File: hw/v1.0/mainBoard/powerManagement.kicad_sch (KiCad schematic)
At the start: 23 parts, among them J10 Conn_01x01, J16 Battery_voltage, J9 Conn_01x01, Q10 AO3401A, Q11 2N7002, Q12 AO3401A, Q13 2N7002, Q9 AO3401A, U3 AMS1117-3.3

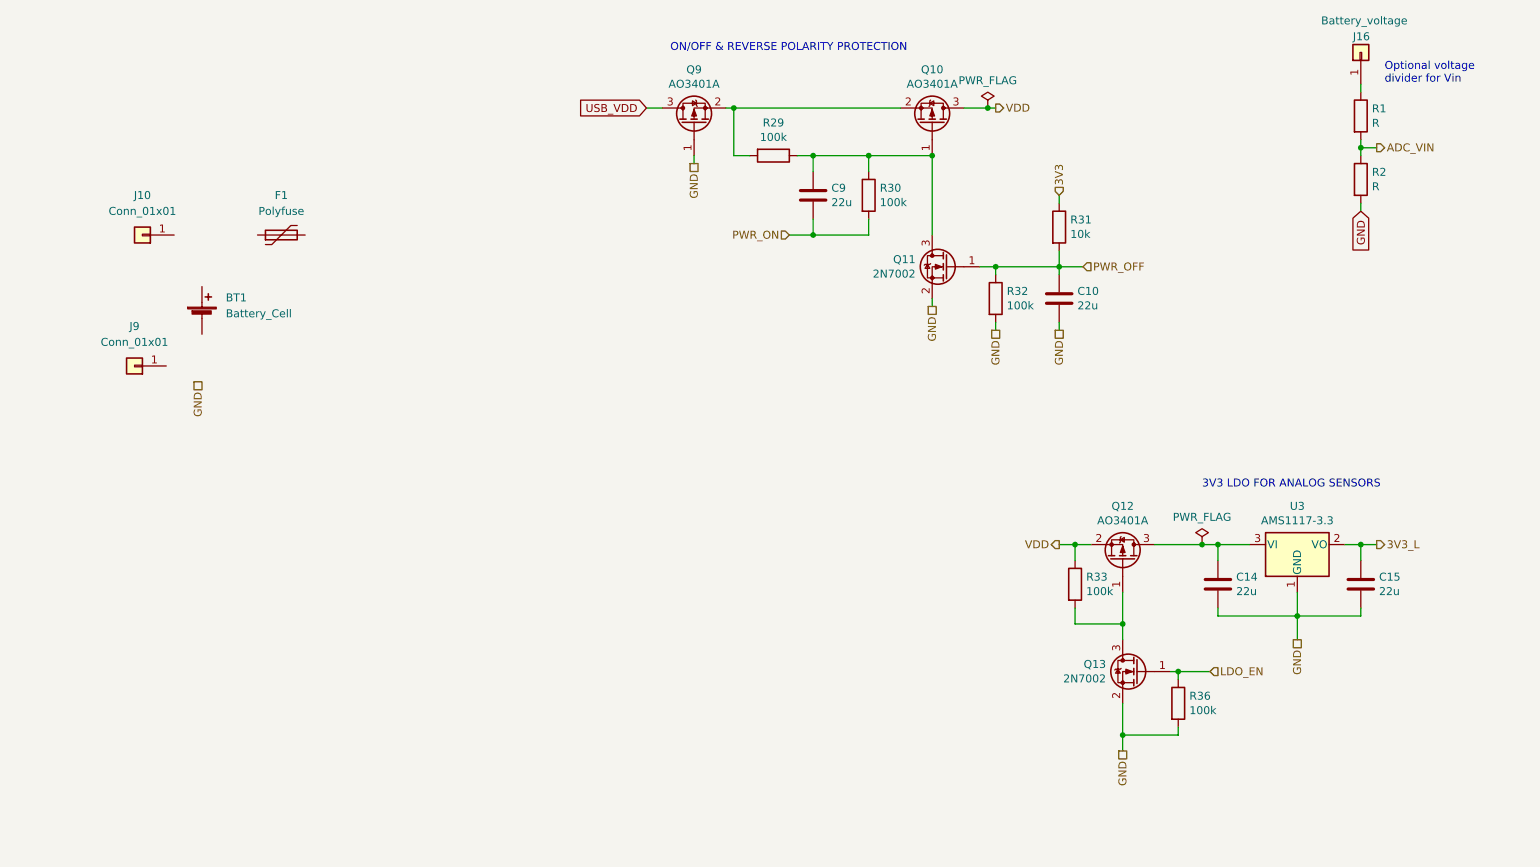
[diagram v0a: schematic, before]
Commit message: Start routing PCB
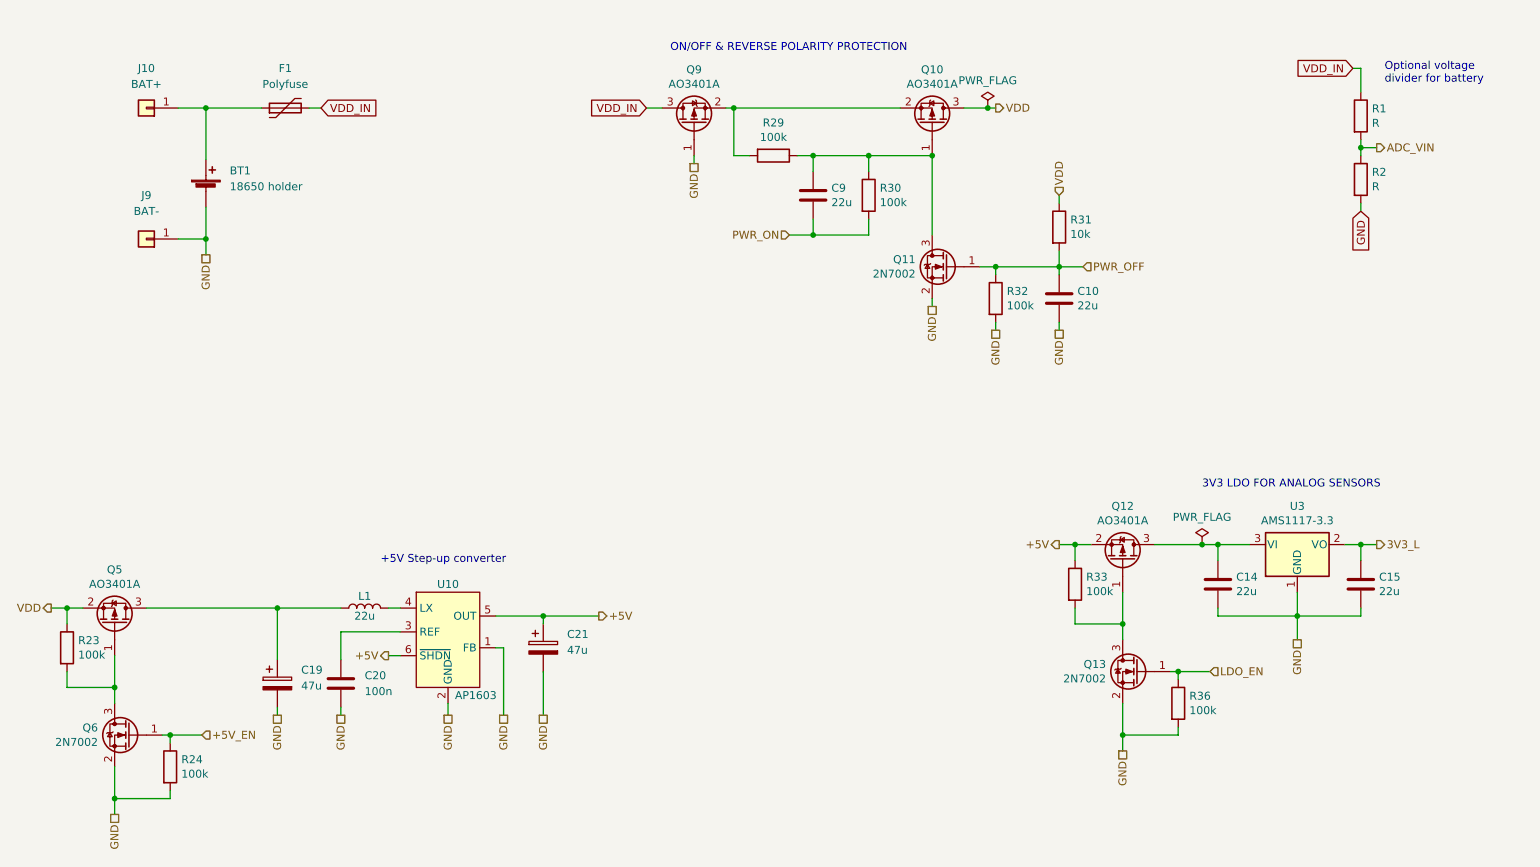
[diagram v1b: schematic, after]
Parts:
- removed J16: Battery_voltage, Connector_PinHeader_2.54mm:PinHeader_1x01_P2.54mm_Vertical, symbol Connector_Generic:Conn_01x01
- added C19, C21: 47u, Capacitor_SMD:CP_Elec_6.3x7.7, symbol Device:C_Polarized
- added C20: 100n, Capacitor_SMD:C_0603_1608Metric, symbol Device:C
- added L1: 22u, Inductor_SMD:L_Coilcraft_LPS4018, symbol Device:L
- added Q5: AO3401A, Package_TO_SOT_SMD:SOT-23, symbol Device:Q_PMOS_GSD
- added Q6: 2N7002, Package_TO_SOT_SMD:SOT-23, symbol Transistor_FET:2N7002
- added R23, R24: 100k, Resistor_SMD:R_0805_2012Metric, symbol Device:R
- added U10: AP1603, Package_TO_SOT_SMD:SOT-23-6_Handsoldering, symbol mainBoard:AP1603
- BT1: value Battery_Cell -> 18650 holder; footprint (none) -> Connector_JST:JST_XH_B2B-XH-A_1x02_P2.50mm_Vertical
- F1: footprint (none) -> Fuse:Fuse_1812_4532Metric_Pad1.30x3.40mm_HandSolder
- J10: value Conn_01x01 -> BAT+; footprint (none) -> mainBoard:2mm_Banana-Socket
- J9: value Conn_01x01 -> BAT-; footprint (none) -> mainBoard:2mm_Banana-Socket
- R29, R30, R31, R32, R33, R36: footprint Resistor_SMD:R_0402_1005Metric -> Resistor_SMD:R_0805_2012Metric
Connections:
- net 3V3 is gone; now on net VDD: R31.1
- net USB_VDD is gone; now on net VDD_IN: Q9.3 (D)
- net GND: now also BT1.2 (-), J9.1 (Pin_1), C19.2, C20.2, C21.2, Q6.2 (S), R24.2, U10.1 (FB), U10.2 (GND)
- net VDD: now also Q5.2 (S), R23.1; no longer Q12.2 (S), R33.1
- net VDD_IN: now reaches R1.1
- net VDD_IN: now also F1.2
- net at J10.1 (Pin_1): now also BT1.1 (+), F1.1
- new net: Q5.1 (G), Q6.3 (D), R23.2
- new net: C19.1, L1.1, Q5.3 (D)
- new net: C20.1, U10.3 (REF)
- new net: L1.2, U10.4 (LX)
- new net +5V: C21.1, Q12.2 (S), R33.1, U10.5 (OUT), U10.6 (~{SHDN})
- new net +5V_EN: Q6.1 (G), R24.1
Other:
- note added: "+5V Step-up converter"
- note added: "Optional voltage divider for battery"
- note removed: "Optional voltage divider for Vin"
- moved on the sheet: BT1, F1, J10, J9

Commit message: Maybe final component placement
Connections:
- net VDD: now also R1.1
- net VDD_IN: no longer R1.1
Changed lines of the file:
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@@
     )
   )
-  (global_label "VDD_IN" (shape input) (at 232.41 27.94 180) (fields_autoplaced)
+  (global_label "VDD" (shape input) (at 232.41 27.94 180) (fields_autoplaced)
     (effects (font (size 1.27 1.27)) (justify right))
-    (property "Intersheet References" "${INTERSHEET_REFS}" (id 0) (at 223.5544 27.8606 0)
+    (property "Intersheet References" "${INTERSHEET_REFS}" (id 0) (at 226.4572 27.8606 0)
       (effects (font (size 1.27 1.27)) (justify right) hide)
     )
